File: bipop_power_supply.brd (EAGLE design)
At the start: 82.5 x 70.8 mm, 32 parts, among them IC1 LM1117MP-3.3, IC2 LM1117MP-5.0, X2 MSTBA6

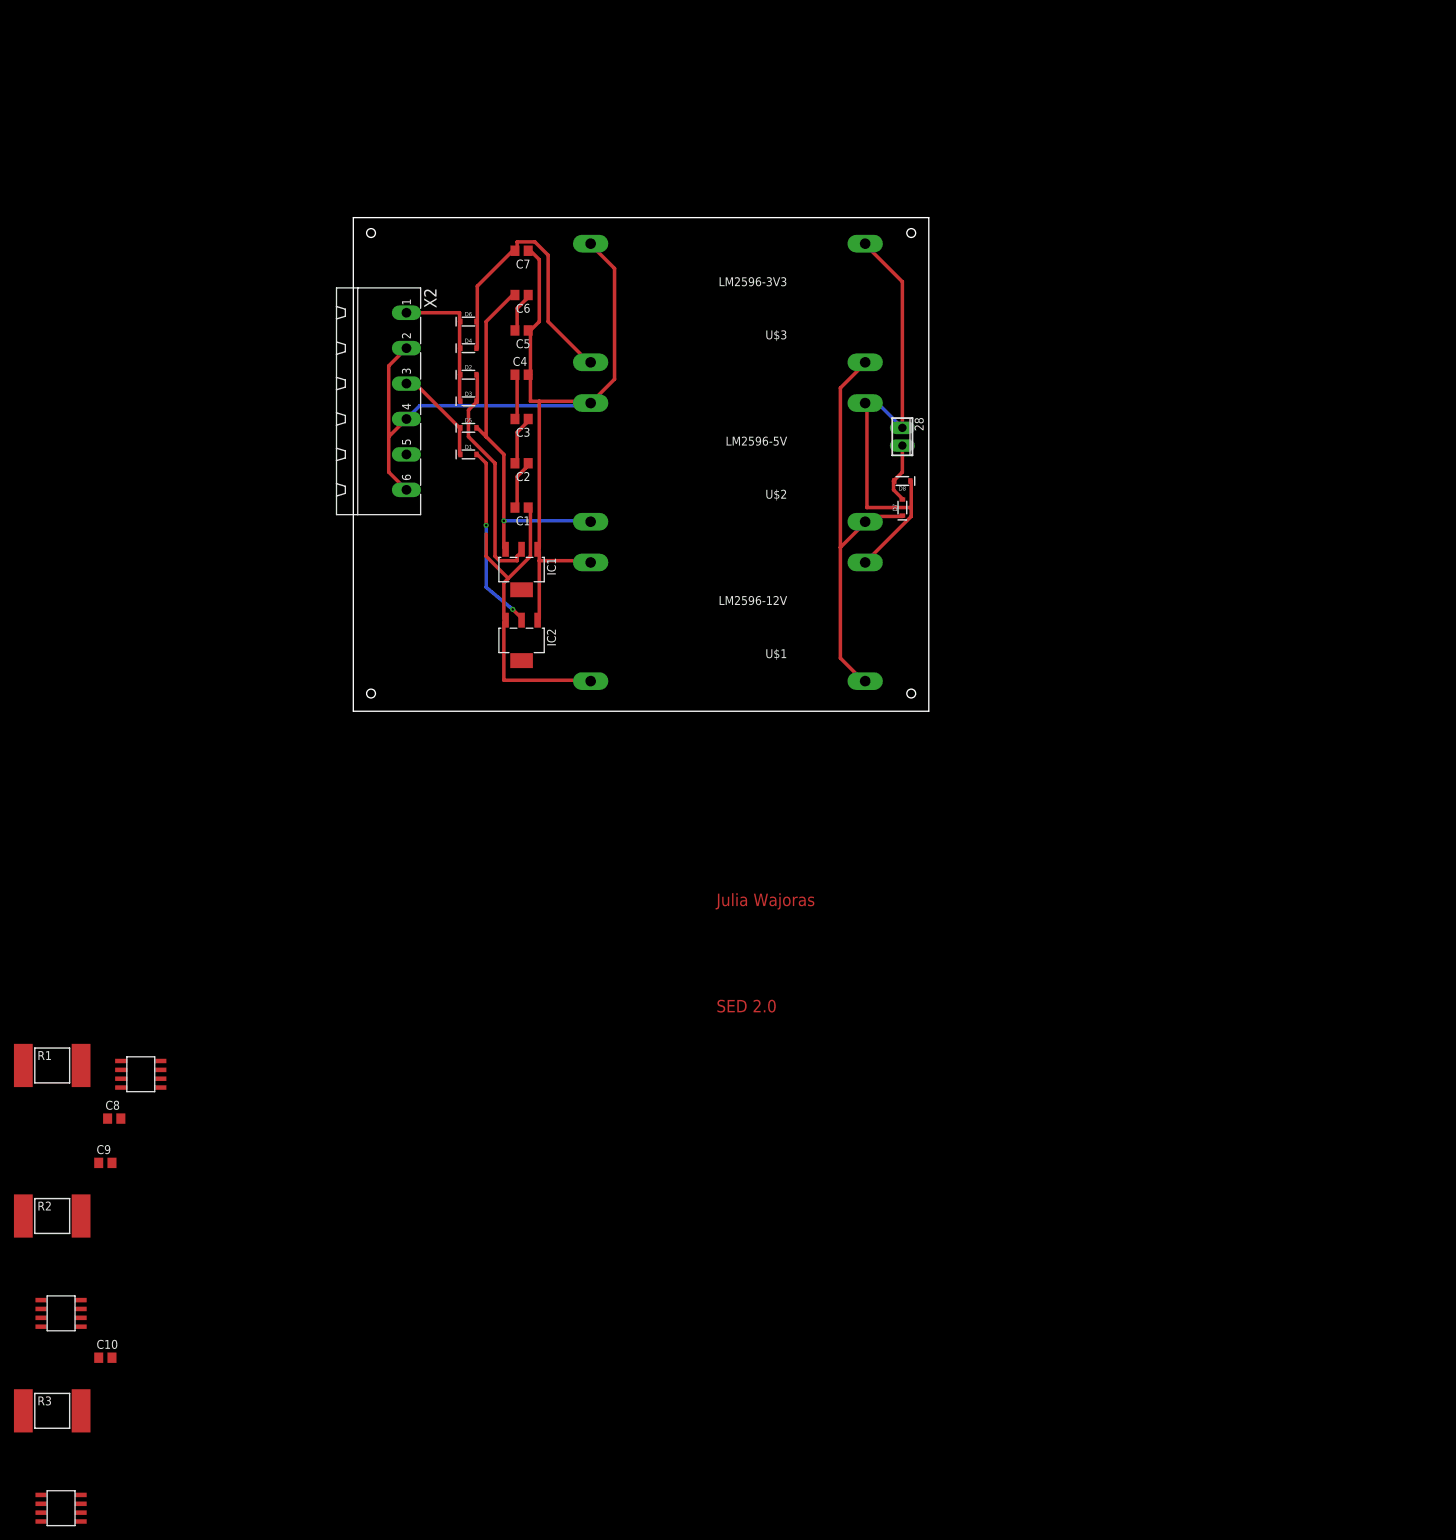
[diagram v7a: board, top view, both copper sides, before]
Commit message: pin interface for current sensors added
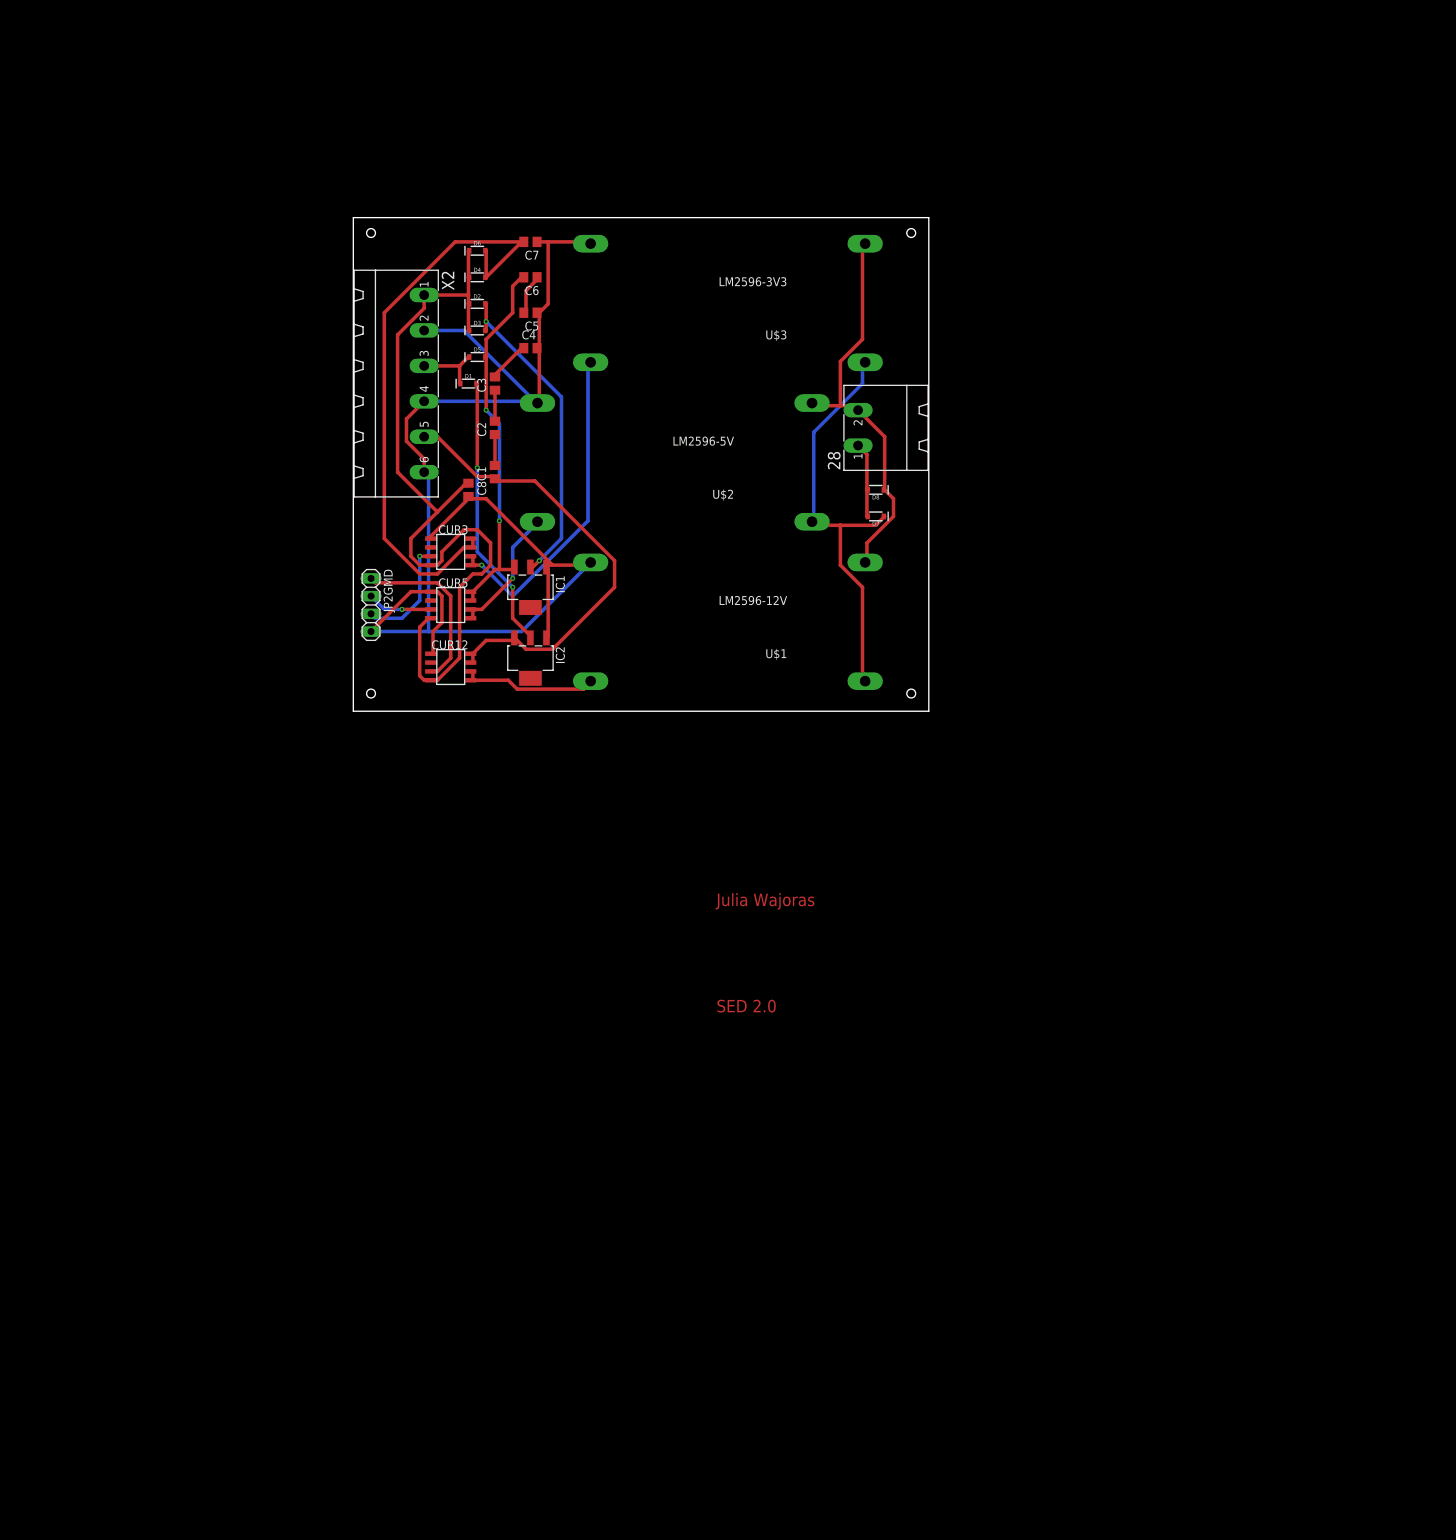
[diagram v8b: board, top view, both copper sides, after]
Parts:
- removed C10, C9: 0.1uF, rcl:C0805
- removed R1, R2, R3: 4.7k, resistor-shunt:BVS
- removed U$5, U$6, U$7: ACS711, lustro_pcb:ACS711
- added CUR12, CUR3, CUR5: ACS711, lustro_pcb:ACS711
- added JP2GMD: (no value), pinhead:1X04
- 28: value (none) -> MSTBA2; device con-phoenix-254:2POL254 -> con-phoenix-508:MSTBA2
- moved C8 103.5 mm to (20.3, 31.8), turned to 270 degrees
- moved D2 10.2 mm to (21.6, 58.4)
- moved D6 10.2 mm to (21.6, 66.0)
- moved D3 10.2 mm to (21.6, 54.6)
- moved D4 10.2 mm to (21.6, 62.2)
- moved D5 10.2 mm to (21.6, 50.8)
- moved D1 10.2 mm to (20.3, 47.0)
- moved U$2 7.62 mm to (50.8, 35.6)
- moved C3 6.35 mm to (24.1, 47.0), turned to 90 degrees
- moved C1 6.35 mm to (24.1, 34.3), turned to 90 degrees
- moved C2 6.35 mm to (24.1, 40.6), turned to 90 degrees
- moved D8 4.02 mm to (78.7, 31.8)
- moved C4 4.02 mm to (29.2, 52.1)
- moved D7 4.02 mm to (78.7, 27.9), turned to 180 degrees
- moved X2 3.59 mm to (8.89, 47.0)
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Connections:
- removed net N$1: R1.2, U$5.FAULT
- removed net N$11: D2.C, D3.C, D4.C, D6.C, X2.1
- removed net N$13: R2.2, U$6.FAULT
- removed net N$14: U$3.V_OUT+
- removed net N$4: R3.2, U$7.FAULT
- new net 3_IN: CUR3.IP+_1, CUR3.IP+_2, U$3.V_OUT+
- new net MM: D7.C, U$1.V_IN+, U$2.V_IN+, U$3.V_IN+
- net 12_IN: now also CUR12.IP+_1, CUR12.IP+_2; no longer C1.1, IC2.3, U$5.IP+_1, U$5.IP+_2
- net 12_OUT: now also C1.1, CUR12.IP-_1, CUR12.IP-_2, IC2.3; no longer U$5.IP-_1, U$5.IP-_2
- net 3_OUT: now also CUR3.IP-_1, CUR3.IP-_2; no longer U$7.IP-_1, U$7.IP-_2
- net 5_IN: now also CUR5.IP+_1, CUR5.IP+_2; no longer C6.2, U$6.IP+_1, U$6.IP+_2
- net 5_OUT: now also C6.2, CUR5.IP-_1, CUR5.IP-_2; no longer U$6.IP-_1, U$6.IP-_2
- net GND: now also CUR12.GND, CUR3.GND, CUR5.GND, JP2GMD.4; no longer C10.2, C9.2, U$5.GND, U$6.GND, U$7.GND
- net N$10: now also 28.2; no longer 28.1
- net N$12: now also 28.1; no longer 28.2
- net VCC_3V3: now also CUR12.VCC, CUR3.VCC, CUR5.VCC, D2.C, D3.C, D4.C, D6.C, X2.1; no longer C10.1, C9.1, D7.C, R1.1, R2.1, R3.1, U$1.V_IN+, U$2.V_IN+, U$3.V_IN+, U$5.VCC, U$6.VCC, U$7.IP+_1, U$7.IP+_2, U$7.VCC
- net VIOUT_12: now also CUR12.VIOUT, JP2GMD.1; no longer U$5.VIOUT
- net VIOUT_3: now also CUR3.VIOUT, JP2GMD.3; no longer U$7.VIOUT
- net VIOUT_5: now also CUR5.VIOUT, JP2GMD.2; no longer U$6.VIOUT
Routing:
- net 12_OUT: track 0.00 -> 66.5 mm
- net MM: track 0.00 -> 61.4 mm
- net VCC_3V3: track 60.0 -> 118.7 mm
- net GND: track 150.5 -> 203.1 mm
- net 3_IN: track 0.00 -> 47.7 mm, vias 0 -> 1
- net 3_OUT: track 41.1 -> 85.9 mm
- net 12_IN: track 46.6 -> 20.0 mm
- net VIOUT_12: track 0.00 -> 25.0 mm
- net N$11: track 20.8 -> 0.00 mm
- net 5_IN: track 0.00 -> 19.1 mm, vias 0 -> 1
- net VIOUT_3: track 0.00 -> 16.3 mm, vias 0 -> 1
- net N$10: track 71.4 -> 57.5 mm
- net N$3: track 26.7 -> 39.7 mm
- net N$5: track 33.7 -> 46.3 mm, vias 0 -> 2
- net VIOUT_5: track 0.00 -> 9.42 mm, vias 0 -> 1
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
